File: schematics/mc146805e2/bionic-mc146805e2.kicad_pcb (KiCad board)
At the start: 2 copper layers, 25.4 x 68.6 mm, 8 parts, among them J1 Bionic-P135, J2 Bionic-P245, U1 MC146805E2P, U2 11AA010-I/TT

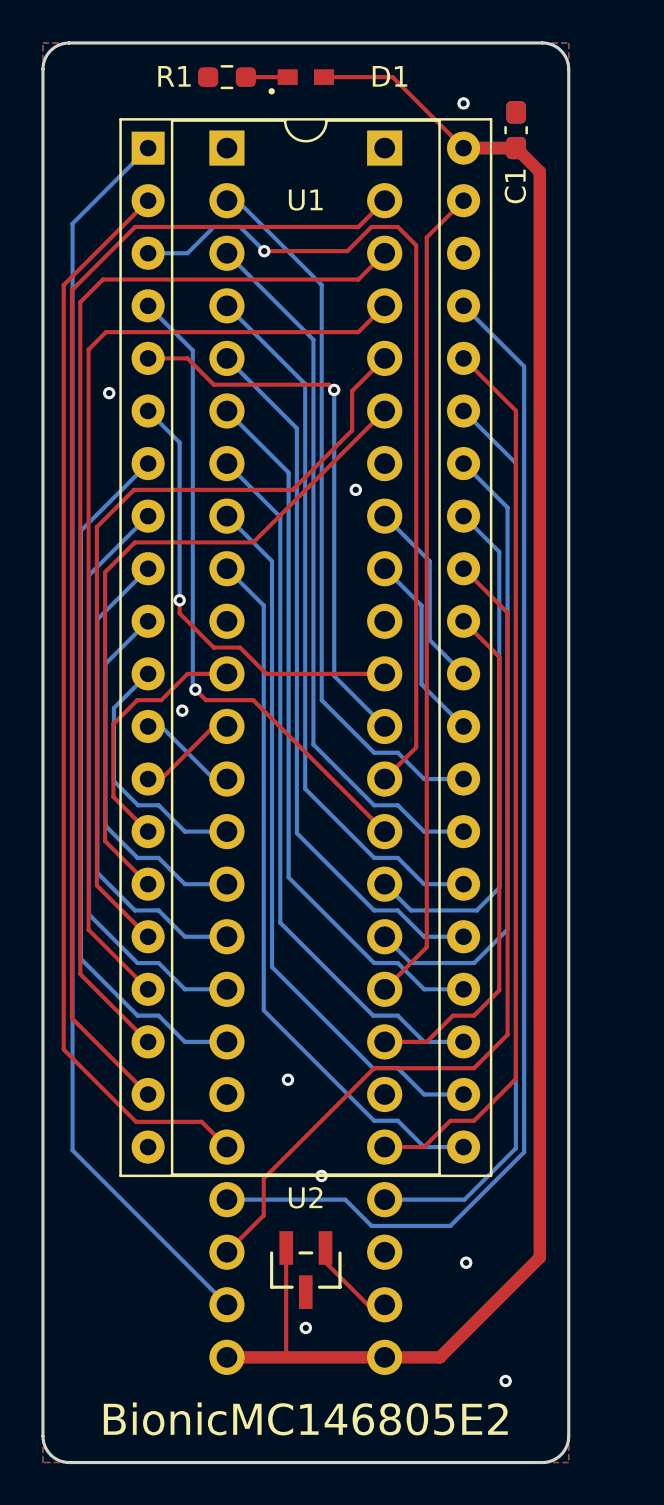
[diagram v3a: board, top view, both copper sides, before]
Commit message: [MC146805E2] Cleanup schematics
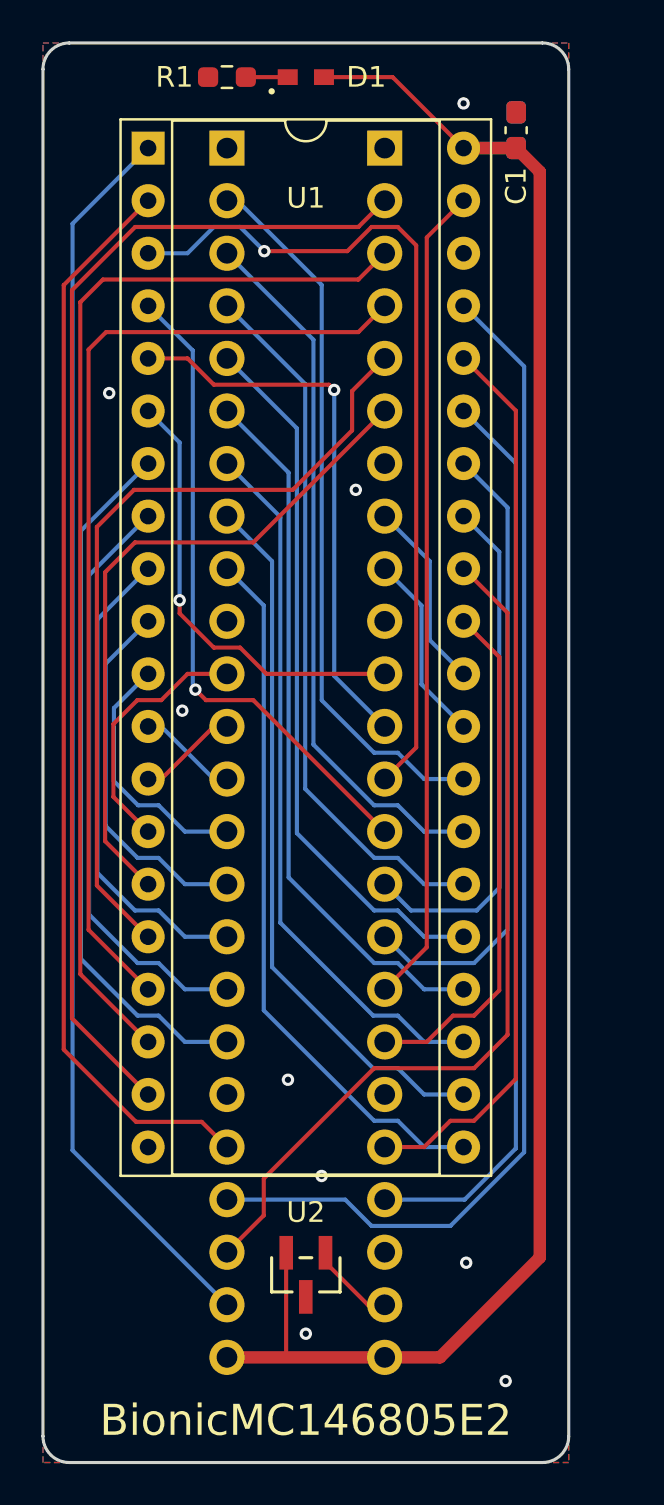
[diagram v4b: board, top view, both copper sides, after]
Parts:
- D1: footprint 0-LocalLibrary:LED_CSL1901UW1_ROM-M -> rhom:LED_CSL1901UW1_ROM-M
- J1: footprint 0-LocalLibrary:Bionic-P135_Vertical -> bionic:Bionic-P135_Vertical
- J2: footprint 0-LocalLibrary:Bionic-P245_Vertical -> bionic:Bionic-P245_Vertical
- U1: footprint 0-LocalLibrary:DIP-40_W15.24mm_Socket -> bionic:DIP-40_W15.24mm_Socket
- U2: footprint 0-LocalLibrary:SOT-23_MC_MCH-M -> microchip:SOT-23_MC_MCH-M
- moved U2 0.23 mm to (113.7, 129.5)
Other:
- rule pad_to_mask_clearance: 0.051 -> 0
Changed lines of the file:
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@@
 	)
 	(setup
-		(pad_to_mask_clearance 0.051)
-		(solder_mask_min_width 0.25)
+		(pad_to_mask_clearance 0)
 		(allow_soldermask_bridges_in_footprints no)
 		(aux_axis_origin 101 70)
@@
 	(net 47 "/P43")
 	(net 48 "/P47")
-	(footprint "0-LocalLibrary:SOT-23_MC_MCH-M"
+	(footprint "microchip:SOT-23_MC_MCH-M"
 		(layer "F.Cu")
-		(at 113.7 129.2828 180)
+		(at 113.7 129.513 180)
 		(descr "Microchip 11AAxxx-I/TT UNI/O 1Kbit Serial EEPROM")
 		(property "Reference" "U2"
-			(at 0 3.4544 0)
+			(at 0 3.0218 0)
 			(unlocked yes)
 			(layer "F.SilkS")
@@
 			)
 		)
-		(property "Footprint" "0-LocalLibrary:SOT-23_MC_MCH-M"
+		(property "Footprint" "microchip:SOT-23_MC_MCH-M"
 			(at 0 0 180)
 			(layer "F.Fab")
@@
 			)
 		)
-		(property "Description" ""
+		(property "Description" "UNI/O Serial EEPROM (1Kbit)"
 			(at 0 0 180)
 			(layer "F.Fab")
@@
 			(pintype "power_in")
 		)
-		(model "${KIPRJMOD}/0-LocalLibrary/SOT-23_MC_MCH.step"
+		(model "${KIPRJMOD}/microchip.pretty/SOT-23_MC_MCH.step"
 			(offset
 				(xyz 0 0 0)
@@
 		)
 	)
-	(footprint "0-LocalLibrary:DIP-40_W15.24mm_Socket"
+	(footprint "bionic:DIP-40_W15.24mm_Socket"
 		(locked yes)
 		(layer "F.Cu")
@@
 		(tags "THT DIP DIL PDIP 2.54mm 15.24mm 600mil Socket")
 		(property "Reference" "U1"
-			(at 7.62 2.54 0)
+			(at 7.62 2.413 0)
 			(layer "F.SilkS")
 			(effects
@@
 			)
 		)
-		(property "Footprint" "0-LocalLibrary:DIP-40_W15.24mm_Socket"
+		(property "Footprint" "bionic:DIP-40_W15.24mm_Socket"
 			(at 0 0 0)
 			(layer "F.Fab")
@@
 			)
 		)
-		(property "Description" ""
+		(property "Description" "8-bit General Purpose Microprocessor, DIP-40"
 			(at 0 0 0)
 			(layer "F.Fab")
@@
 		)
 	)
-	(footprint "0-LocalLibrary:LED_CSL1901UW1_ROM-M"
+	(footprint "rhom:LED_CSL1901UW1_ROM-M"
 		(layer "F.Cu")
 		(at 113.7 71.651)
@@
 		(tags "CSL1901UW1 ")
 		(property "Reference" "D1"
-			(at 4.064 0 0)
+			(at 2.921 0 0)
 			(unlocked yes)
 			(layer "F.SilkS")
@@
 			)
 		)
-		(property "Footprint" "0-LocalLibrary:LED_CSL1901UW1_ROM-M"
+		(property "Footprint" "rhom:LED_CSL1901UW1_ROM-M"
 			(at 0 0 0)
 			(layer "F.Fab")
@@
 			)
 		)
+		(model "${KIPRJMOD}/rhom.pretty/LED_CSL1901UW1_ROM.step"
+			(offset
+				(xyz 0 0 0)
+			)
+			(scale
+				(xyz 1 1 1)
+			)
+			(rotate
+				(xyz 0 0 0)
+			)
+		)
 	)
 	(footprint "Capacitor_SMD:C_0603_1608Metric_Pad1.08x0.95mm_HandSolder"
@@
 		)
 	)
-	(footprint "0-LocalLibrary:Bionic-P245_Vertical"
+	(footprint "bionic:Bionic-P245_Vertical"
 		(locked yes)
 		(layer "B.Cu")
@@
 			)
 		)
-		(property "Footprint" "0-LocalLibrary:Bionic-P245_Vertical"
+		(property "Footprint" "bionic:Bionic-P245_Vertical"
 			(at 0 0 0)
 			(layer "B.Fab")
@@
 			)
 		)
-		(property "Description" ""
+		(property "Description" "Generic connector, single row, 01x24, script generated (kicad-library-utils/schlib/autogen/connector/)"
 			(at 0 0 0)
 			(layer "B.Fab")
@@
 		)
 	)
-	(footprint "0-LocalLibrary:Bionic-P135_Vertical"
+	(footprint "bionic:Bionic-P135_Vertical"
 		(locked yes)
 		(layer "B.Cu")
@@
 			)
 		)
-		(property "Footprint" "0-LocalLibrary:Bionic-P135_Vertical"
+		(property "Footprint" "bionic:Bionic-P135_Vertical"
 			(at 0 0 0)
 			(layer "B.Fab")
@@
 			)
 		)
-		(property "Description" ""
+		(property "Description" "Generic connector, single row, 01x24, script generated (kicad-library-utils/schlib/autogen/connector/)"
 			(at 0 0 0)
 			(layer "B.Fab")
@@
 	)
 	(segment
+		(start 112.749999 128.447)
+		(end 112.749999 133.434001)
+		(width 0.2)
+		(layer "F.Cu")
+		(net 1)
+	)
+	(segment
 		(start 114.5763 71.651)
 		(end 117.891 71.651)
@@
 	)
 	(segment
-		(start 112.749999 128.2168)
-		(end 112.749999 133.434001)
-		(width 0.2)
-		(layer "F.Cu")
-		(net 1)
-	)
-	(segment
 		(start 120.177 133.5)
 		(end 117.51 133.5)
@@
 	)
 	(via
-		(at 113.7 132.0776)
+		(at 113.7 132.357)
 		(size 0.6)
 		(drill 0.3)
@@
 	)
 	(segment
-		(start 116.6972 130.96)
-		(end 117.51 130.96)
+		(start 114.650001 128.447)
+		(end 114.650001 128.912801)
 		(width 0.2)
 		(layer "F.Cu")
@@
 	)
 	(segment
-		(start 114.650001 128.2168)
-		(end 114.650001 128.912801)
+		(start 116.6972 130.96)
+		(end 117.51 130.96)
 		(width 0.2)
 		(layer "F.Cu")

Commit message: [MC146805E2] Update schematics
Remove unused pins from bionic connector
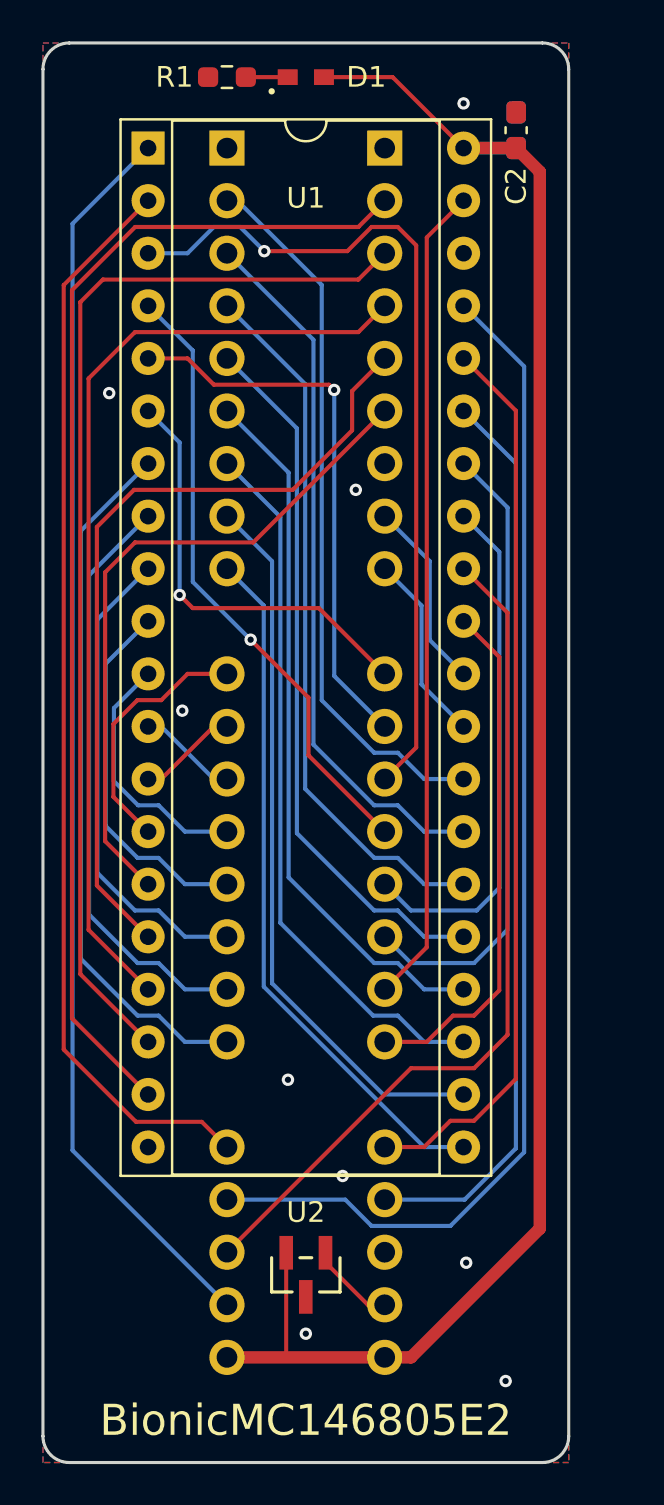
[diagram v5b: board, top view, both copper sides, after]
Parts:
- C1: moved to B.Cu
- C2: moved to F.Cu
- J1: footprint bionic:Bionic-P135_Vertical -> bionic:Bionic-P135_THT
- J2: footprint bionic:Bionic-P245_Vertical -> bionic:Bionic-P245_THT
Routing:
- net /P43: track 31.5 -> 30.1 mm
- net /P52: track 42.3 -> 41.3 mm
- net VCC: track 89.4 -> 88.6 mm
- net /P22: track 47.3 -> 46.5 mm
- net /P17: track 34.5 -> 33.8 mm
- net /P40: track 21.5 -> 21.0 mm
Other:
- board text added: "Rev. 9"
- board text removed: "Rev. 8"
